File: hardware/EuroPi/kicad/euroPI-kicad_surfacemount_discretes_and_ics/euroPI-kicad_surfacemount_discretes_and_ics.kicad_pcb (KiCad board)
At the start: 2 copper layers, 121.9 x 128.5 mm, 105 parts, among them J1 Output 1 Jack, J10 Eurorack Power 2x8 16p, J11 Conn_01x13_Socket, J12 OLED 64x128, J13 USB_B_Micro, J14 Conn_01x03_Pin, J15 Conn_01x04_Pin, J16 Conn_02x04_Top_Bottom, J17 Conn_01x13_Pin, J18 Conn_01x04_Pin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

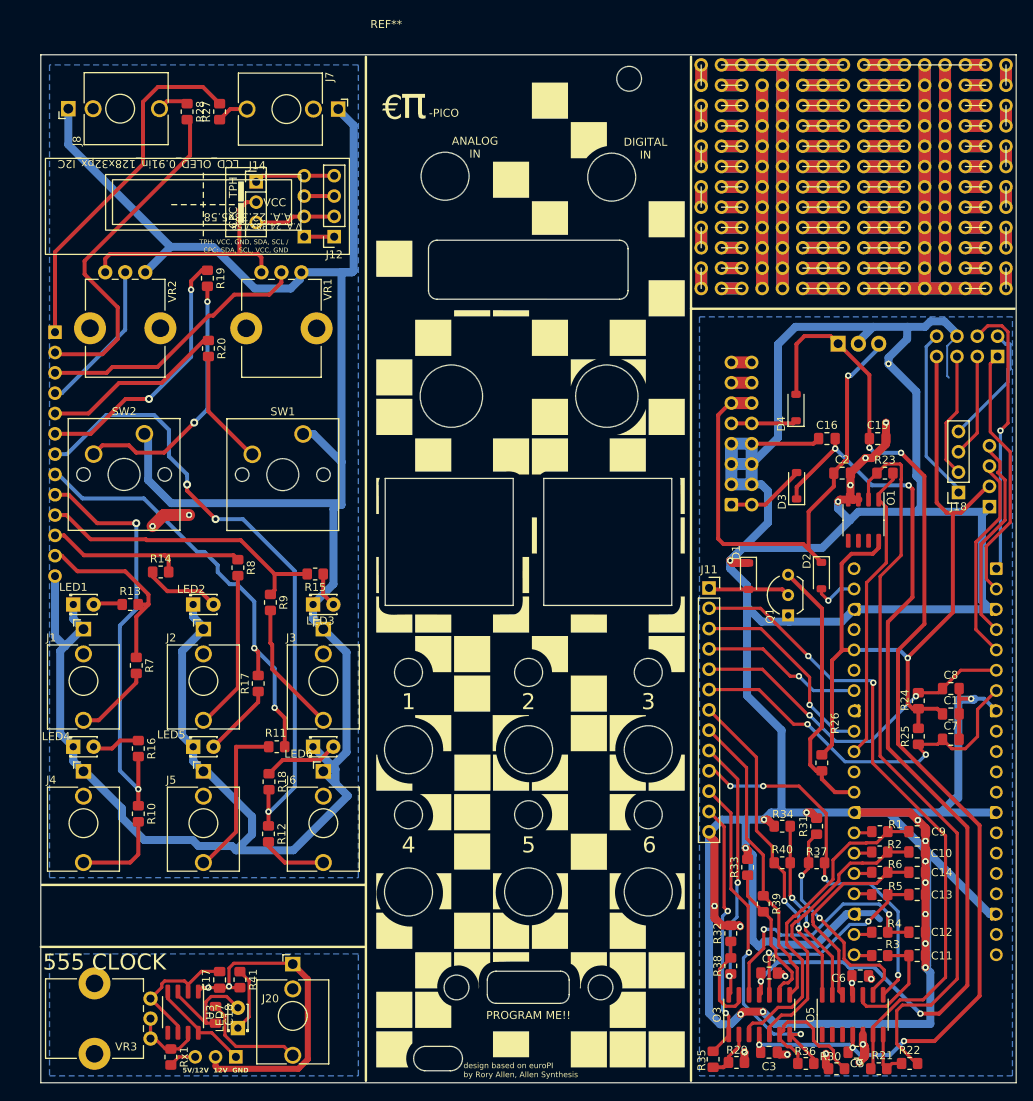
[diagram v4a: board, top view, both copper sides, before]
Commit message: some updates of smt version incl correcting layout component choices support structures
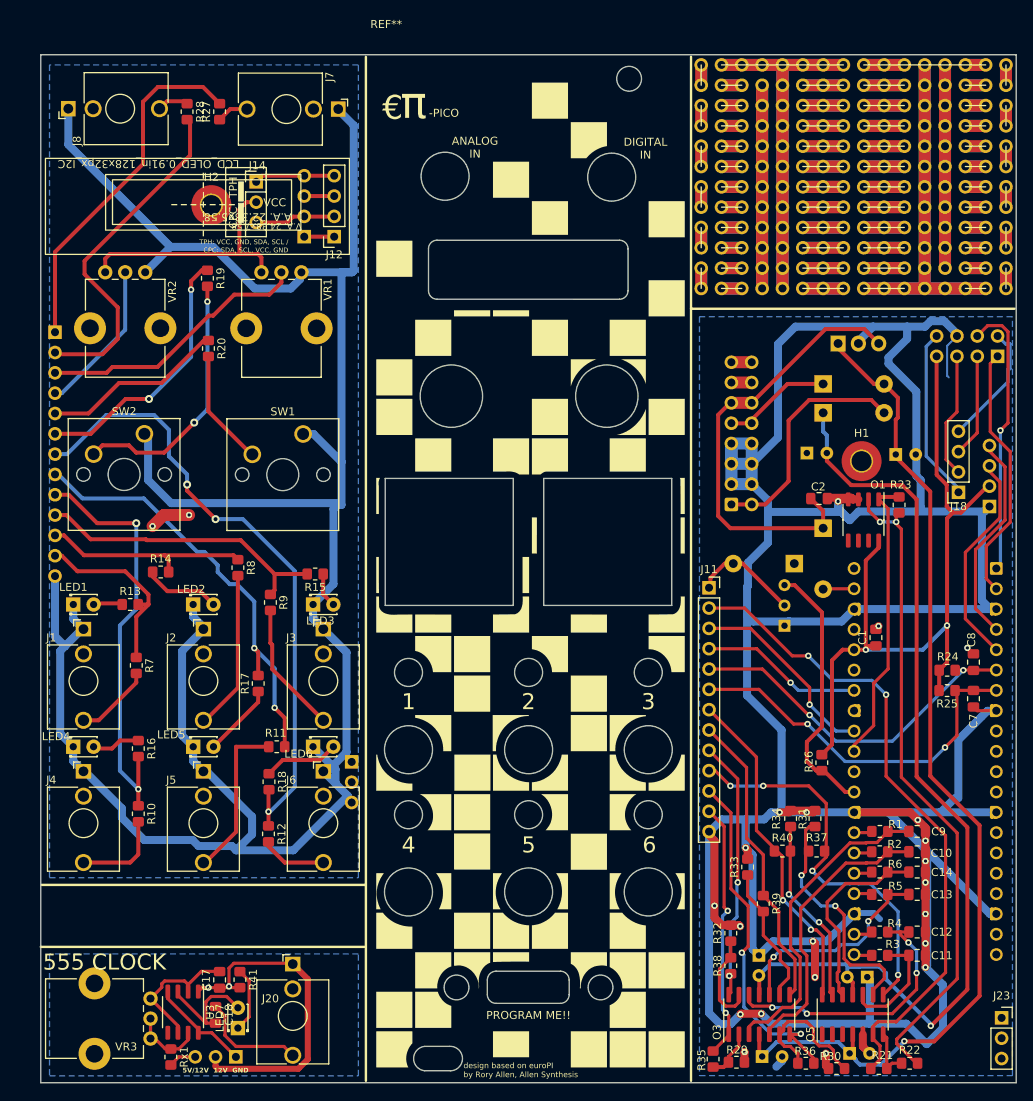
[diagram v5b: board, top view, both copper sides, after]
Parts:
- added H1: MountingHole_Pad, MountingHole:MountingHole_2.5mm_Pad_TopOnly, F.Cu at (183.9, 76.2)
- added H2: MountingHole_Pad, MountingHole:MountingHole_2.5mm_Pad_TopOnly, F.Cu at (102.6, 44.2)
- added J22: Conn_01x03_Pin, Connector_PinHeader_2.54mm:PinHeader_1x03_P2.54mm_Vertical, B.Cu at (120.1, 113.8)
- added J23: Conn_01x03_Socket, Connector_PinSocket_2.54mm:PinSocket_1x03_P2.54mm_Vertical, F.Cu at (201.4, 145.8)
- C15, C16, C3, C4, C5, C6: footprint Capacitor_SMD:C_0805_2012Metric_Pad1.18x1.45mm_HandSolder -> Library:CP_Radial_D5.0mm_P2.50mm; moved to B.Cu
- D1, D2, D3, D4: value 1N4448W -> 1N5817 Schottky Diode; footprint Diode_SMD:D_SOD-123 -> Diode_THT:D_DO-41_SOD81_P7.62mm_Horizontal; moved to B.Cu
- J15: value Conn_01x04_Pin -> I2C aux
- Q1: moved to B.Cu
- moved C1 13.4 mm to (185.7, 98.3), turned to 90 degrees
- moved D3 9.70 mm to (179.1, 70.2), turned to 0 degrees
- moved R25 6.75 mm to (194.6, 104.9), turned to 180 degrees
- moved D1 5.94 mm to (175.5, 89.0), turned to 180 degrees
- moved D2 5.92 mm to (179.1, 84.6)
- moved C7 5.82 mm to (197.9, 105.9), turned to -90 degrees
- moved R24 5.25 mm to (194.6, 102.3), turned to 180 degrees
- moved D4 4.49 mm to (179.1, 66.5), turned to 0 degrees
- moved C8 4.35 mm to (197.9, 101.3), turned to 90 degrees
- moved R23 4.35 mm to (188.6, 81.7), turned to 90 degrees
- moved C2 4.29 mm to (178.6, 80.9)
- moved C16 3.09 mm to (177.0, 75.2)
- moved C15 3.00 mm to (188.1, 75.4)
- moved C4 2.55 mm to (171.0, 138.0), turned to -90 degrees
- moved R40 1.46 mm to (174.0, 124.9)
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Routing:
- net I2C_GND: track 849.1 -> 825.5 mm, vias 30 -> 23
- net Net-(D3-K): track 10.1 -> 29.7 mm
- net ~: track 154.0 -> 139.2 mm, vias 5 -> 1
- net Net-(O1A--): track 93.6 -> 82.0 mm, vias 0 -> 2
- net +5V: track 67.7 -> 59.5 mm, vias 1 -> 0
- net -12V: track 129.2 -> 121.7 mm, vias 5 -> 1
- net I2C_VCC: track 131.8 -> 124.5 mm, vias 1 -> 2
- net Net-(D4-A): track 8.20 -> 13.5 mm
- net CJD: track 54.8 -> 58.1 mm
- net Net-(O3D-+): track 32.0 -> 34.4 mm, vias 2 -> 4
- net CJ3: track 84.5 -> 86.9 mm
- net CS2: track 81.4 -> 79.7 mm
- net Net-(D2-K): track 5.65 -> 4.13 mm, vias 1 -> 0
- net Net-(O5D-+): track 25.8 -> 24.3 mm
- net Net-(O5C--): track 28.1 -> 29.5 mm
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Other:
- board text added: "COMPONENTS HERE ONLY NEEDED IF +5V INPUT N/A"
